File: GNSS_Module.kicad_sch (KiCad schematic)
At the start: 31 parts, among them J301 GNSS_MAINBOARD_CONN, J302 GNSS_MODULE_BOARD_CONNECTOR, J303 GNSS_FTDI_CONN, U301 SAM-M8Q

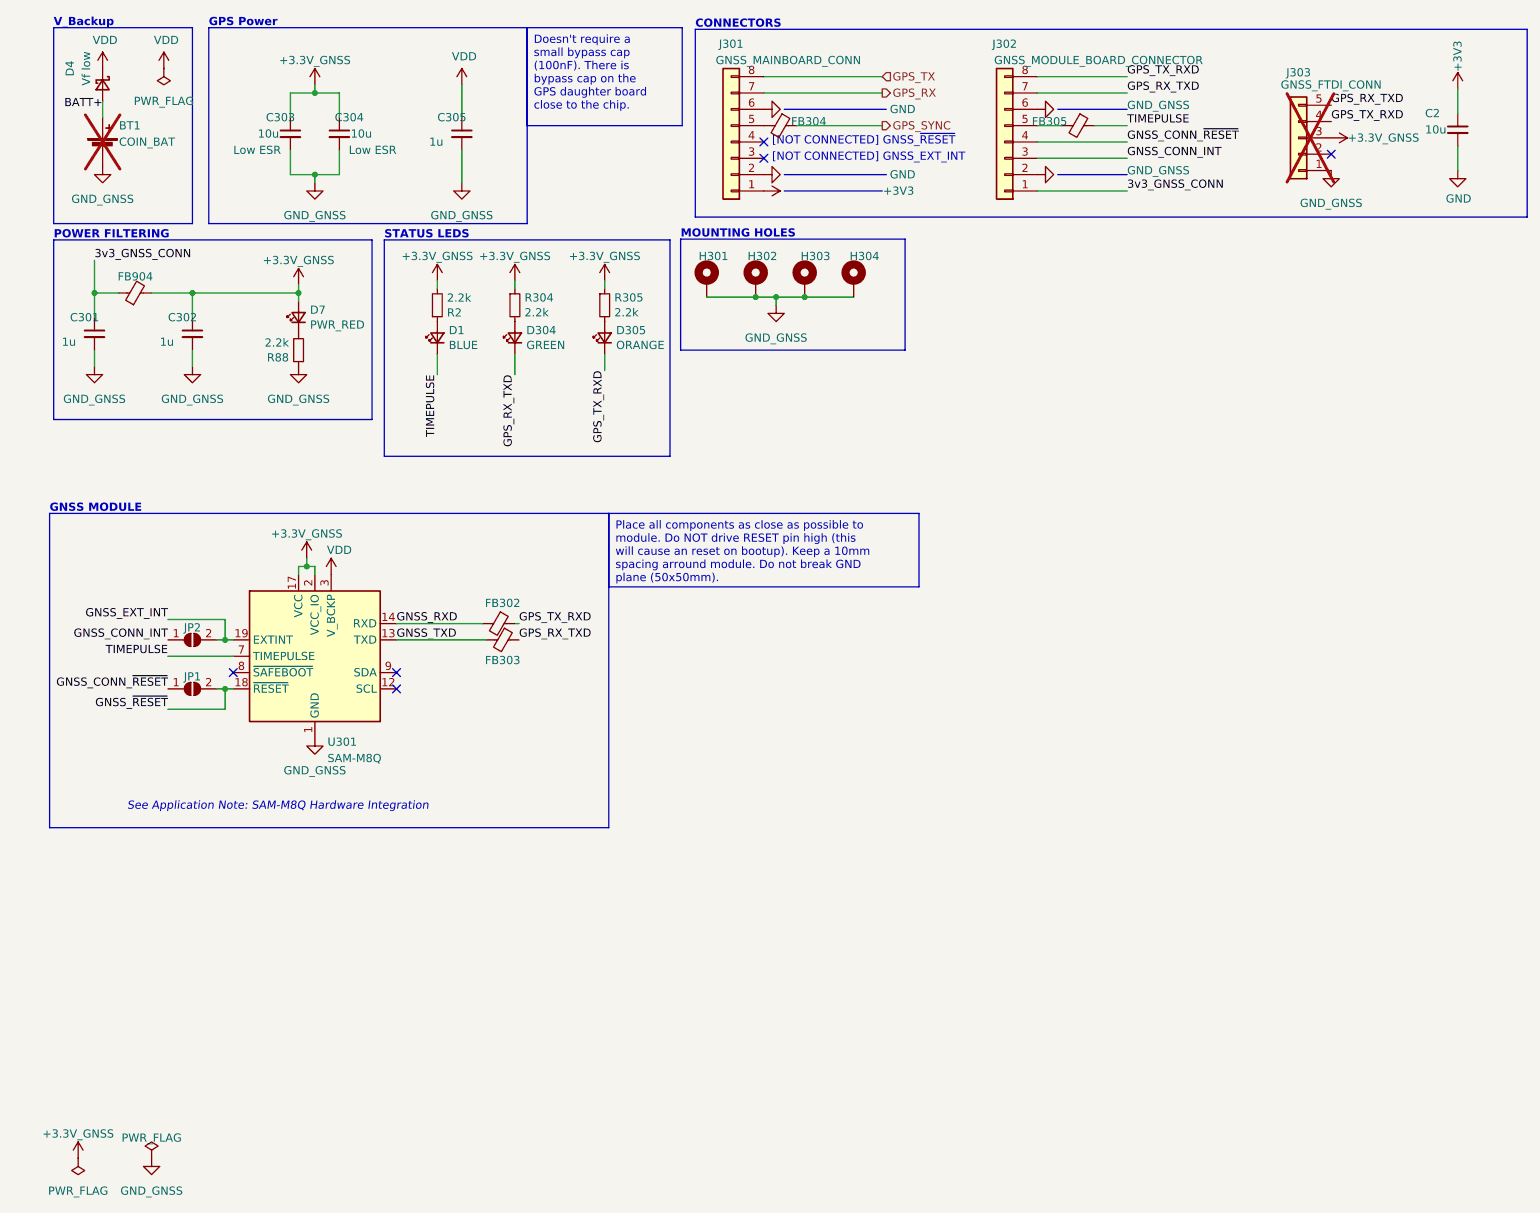
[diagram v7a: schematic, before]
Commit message: (sch) consoldate BOM
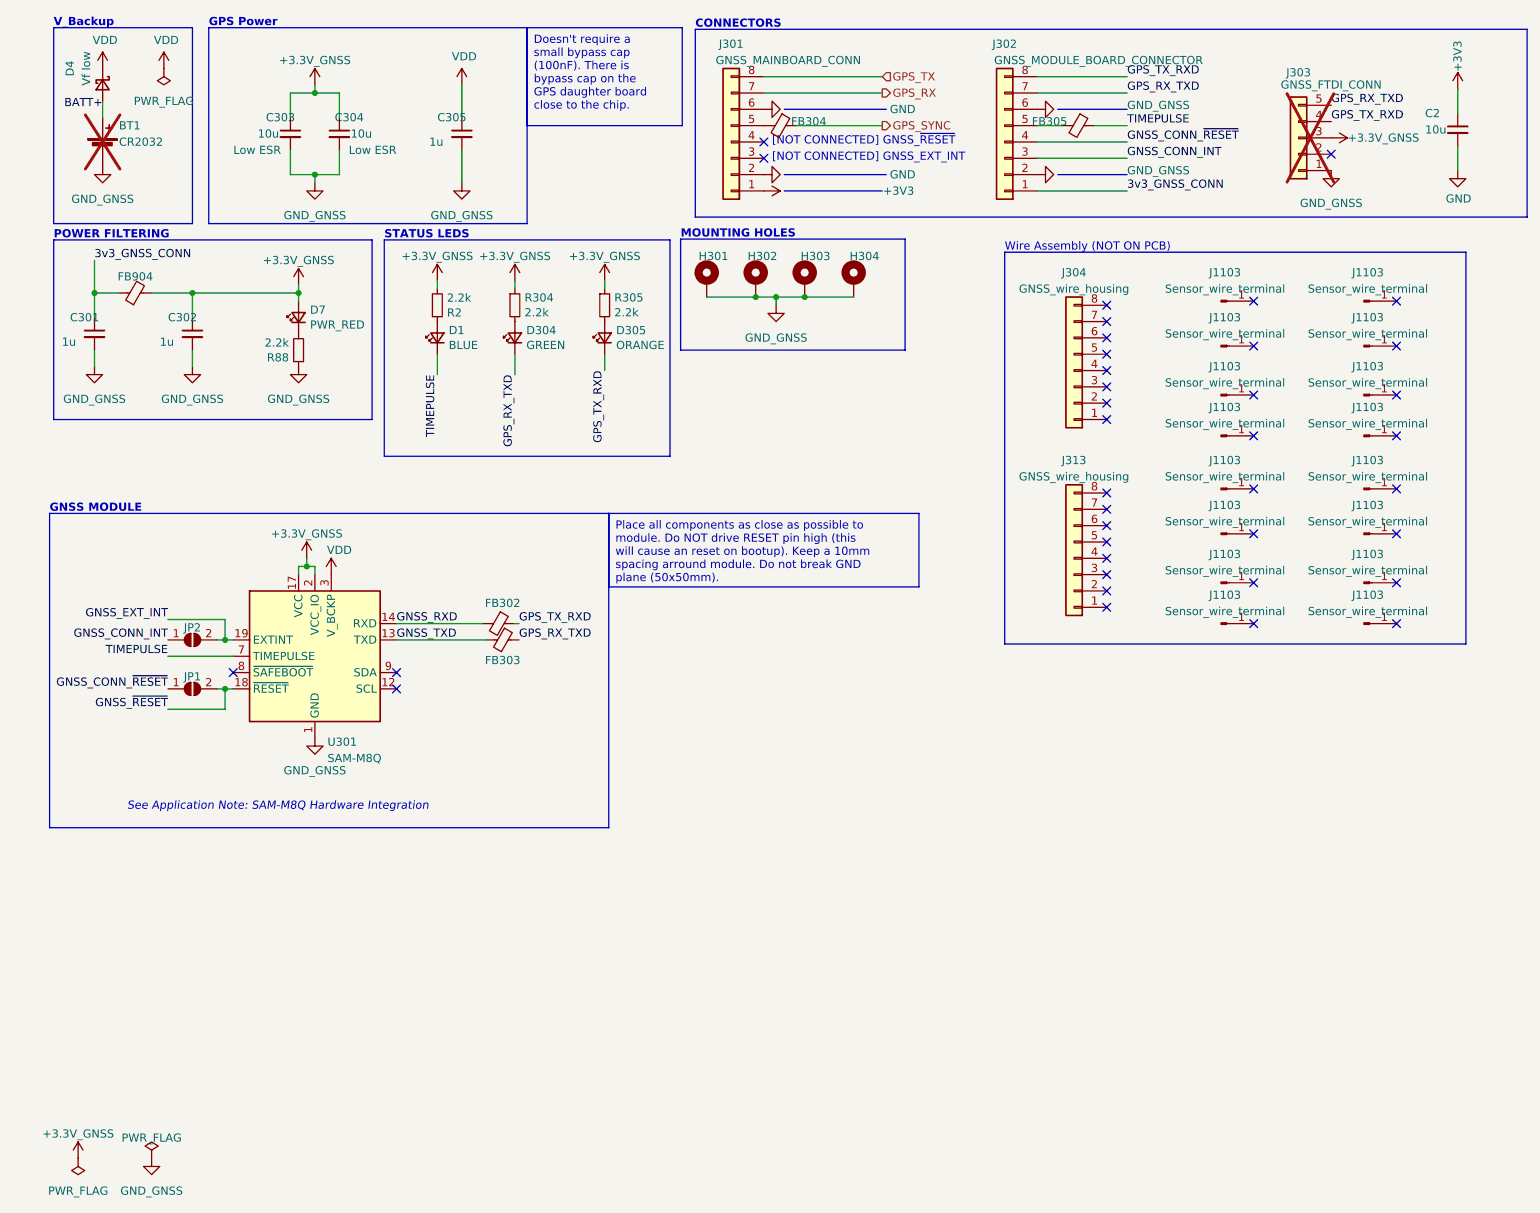
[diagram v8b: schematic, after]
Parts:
- added J1103 (x16): Sensor_wire_terminal, symbol Connector:Conn_01x01_Pin
- added J304, J313: GNSS_wire_housing, symbol Connector_Generic:Conn_01x08
- BT1: value COIN_BAT -> CR2032
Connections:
- no-connect marks 6 -> 38
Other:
- note added: "Wire Assembly (NOT ON PCB)"
